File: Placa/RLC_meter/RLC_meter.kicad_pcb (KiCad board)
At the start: 2 copper layers, 12 parts, among them J1 BAT, J2 BAT, Q1 IRF4905, Q2 IRF4905, U3 L7805, U4 LM358

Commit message: massive update. Local to git
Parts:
- removed Q1, Q2: IRF4905, Package_TO_SOT_THT:TO-220-3_Vertical
- removed REF**: TP4056 module, RLC_meter:TP4056
- added C3: 100n, Capacitor_THT:C_Disc_D5.0mm_W2.5mm_P2.50mm, F.Cu at (34.0, 63.8)
- added C4: 100n, Capacitor_THT:C_Disc_D5.0mm_W2.5mm_P2.50mm, F.Cu at (43.0, 63.8)
- added C5: 100u, Capacitor_THT:CP_Radial_D8.0mm_P5.00mm, F.Cu at (47.1, 64.5)
- added J3: HC05, Connector_PinHeader_2.54mm:PinHeader_1x04_P2.54mm_Horizontal, F.Cu at (94.6, 22.7)
- added J4: Load_terminal, TerminalBlock_Philmore:TerminalBlock_Philmore_TB132_1x02_P5.00mm_Horizontal, F.Cu at (31.2, 37.0)
- added R4: 100k, Resistor_THT:R_Axial_DIN0309_L9.0mm_D3.2mm_P15.24mm_Horizontal, F.Cu at (55.9, 23.0)
- added R5: 560, Resistor_THT:R_Axial_DIN0309_L9.0mm_D3.2mm_P15.24mm_Horizontal, F.Cu at (60.0, 26.9)
- added R6: 560, Resistor_THT:R_Axial_DIN0309_L9.0mm_D3.2mm_P15.24mm_Horizontal, F.Cu at (89.1, 23.0)
- added RV1: 50k, Potentiometer_THT:Potentiometer_Bourns_3386C_Horizontal, F.Cu at (49.5, 27.5)
- added U1: LPC845, RLC_meter:LPC845, F.Cu at (80.8, 56.9)
- added U2: X9Cxxx, Package_DIP:DIP-8_W7.62mm_Socket_LongPads, F.Cu at (85.3, 34.7)
- added U5: AMS1117-3.3, Connector_PinHeader_2.54mm:PinHeader_1x03_P2.54mm_Vertical, F.Cu at (47.0, 43.5)
- C1, C2: value C -> 100n; footprint Capacitor_THT:C_Axial_L5.1mm_D3.1mm_P7.50mm_Horizontal -> Capacitor_THT:C_Disc_D5.0mm_W2.5mm_P2.50mm
- J1: value BAT -> Batt1
- J2: value BAT -> Batt2
- R1: value R -> 150k; footprint Resistor_THT:R_Axial_DIN0207_L6.3mm_D2.5mm_P10.16mm_Horizontal -> Resistor_THT:R_Axial_DIN0309_L9.0mm_D3.2mm_P15.24mm_Horizontal
- R2: value R -> 220k; footprint Resistor_THT:R_Axial_DIN0207_L6.3mm_D2.5mm_P10.16mm_Horizontal -> Resistor_THT:R_Axial_DIN0309_L9.0mm_D3.2mm_P15.24mm_Horizontal
- R3: value R -> 100k; footprint Resistor_THT:R_Axial_DIN0207_L6.3mm_D2.5mm_P10.16mm_Horizontal -> Resistor_THT:R_Axial_DIN0309_L9.0mm_D3.2mm_P15.24mm_Horizontal
- U3: value L7805 -> MC33202; footprint Package_TO_SOT_THT:TO-220-3_Horizontal_TabDown -> Package_DIP:DIP-8_W7.62mm_Socket_LongPads
- U4: value LM358 -> L7805; footprint Package_DIP:DIP-8_W7.62mm -> Package_TO_SOT_THT:TO-220-3_Horizontal_TabDown
- moved J2 65.7 mm to (29.0, 48.3), turned to 180 degrees
- moved C1 59.2 mm to (38.5, 63.8), turned to -90 degrees
- moved R1 57.7 mm to (28.4, 27.0)
- moved J1 54.0 mm to (29.0, 55.2)
- moved U4 40.1 mm to (35.5, 60.2)
- moved R2 32.1 mm to (43.6, 23.0), turned to 180 degrees
- moved R3 31.1 mm to (63.9, 30.0)
- moved C2 26.2 mm to (45.5, 57.0), turned to -90 degrees
- moved U3 25.1 mm to (72.0, 34.2), turned to -90 degrees
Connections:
- C1 pad 1: +BATT -> +5V
- C2 pad 1: VCC -> +3.3V
- J1 pad 1: Net-(J1-Pad1) -> +BATT
- J1 pad 2: /in_BAT2- -> GND
- J2 pad 1: Net-(J2-Pad1) -> GND
- J2 pad 2: /in_BAT1- -> -BATT
- R2 pad 2: /Signal_o -> -BATT
- R3 pad 1: /Singal_i -> Net-(R3-Pad1)
- R3 pad 2: /Signal_o -> /V_DAC
- U3 pad 1: +BATT -> /Signal_i
- U3 pad 2: GND -> Net-(R3-Pad1)
- U3 pad 3: VCC -> GND
- U4 pad 1: /Signal_o -> +BATT
- U4 pad 2: Net-(R1-Pad2) -> GND
- U4 pad 3: /DAC -> +5V
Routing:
- net +5V: track 0.00 -> 202.0 mm, vias 0 -> 2
- net /Signal_i: track 0.00 -> 112.6 mm
- net /V_DAC: track 0.00 -> 99.1 mm, vias 0 -> 2
- net +BATT: track 0.00 -> 73.5 mm
- net -BATT: track 0.00 -> 69.8 mm
- net /RX: track 0.00 -> 69.4 mm
- net /TX: track 0.00 -> 66.1 mm
- net Net-(R3-Pad1): track 0.00 -> 40.8 mm
- net /generated_signal: track 0.00 -> 37.5 mm
- net /POT+: track 0.00 -> 33.1 mm
- net +3.3V: track 0.00 -> 23.6 mm
- net /POT_V: track 0.00 -> 19.7 mm
- net /POT_U/D: track 0.00 -> 19.3 mm
- net /POT_INC: track 0.00 -> 17.9 mm
- net Net-(R1-Pad2): track 0.00 -> 10.1 mm
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- added copper zone on B.Cu, net GND
- added copper zone on F.Cu, net GND
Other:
- board outline added: 90 x 50 mm

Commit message: correxiones en clase
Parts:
- moved C2 13.0 mm to (58.4, 55.9)
- moved R6 6.57 mm to (82.5, 23.0)
- moved R4 6.35 mm to (49.5, 23.0)
- moved J3 5.02 mm to (89.6, 22.7)
- moved C3 2.95 mm to (31.1, 63.5)
- moved C1 2.95 mm to (35.6, 63.5)
- moved C4 2.95 mm to (40.1, 63.5)
- moved C5 2.51 mm to (44.6, 64.5)
- moved R3 2.06 mm to (63.9, 27.9)
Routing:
- net +5V: track 202.0 -> 223.9 mm
- net /RX: track 69.4 -> 85.0 mm
- net /TX: track 66.1 -> 81.7 mm
- net /Signal_i: track 112.6 -> 120.9 mm
- net +3.3V: track 23.6 -> 19.5 mm
- net /POT+: track 33.1 -> 35.8 mm
- net Net-(R3-Pad1): track 40.8 -> 43.0 mm
- net /V_DAC: track 99.1 -> 101.3 mm, vias 2 -> 0
- net Net-(R1-Pad2): track 10.1 -> 11.7 mm
- net +BATT: track 73.5 -> 74.6 mm

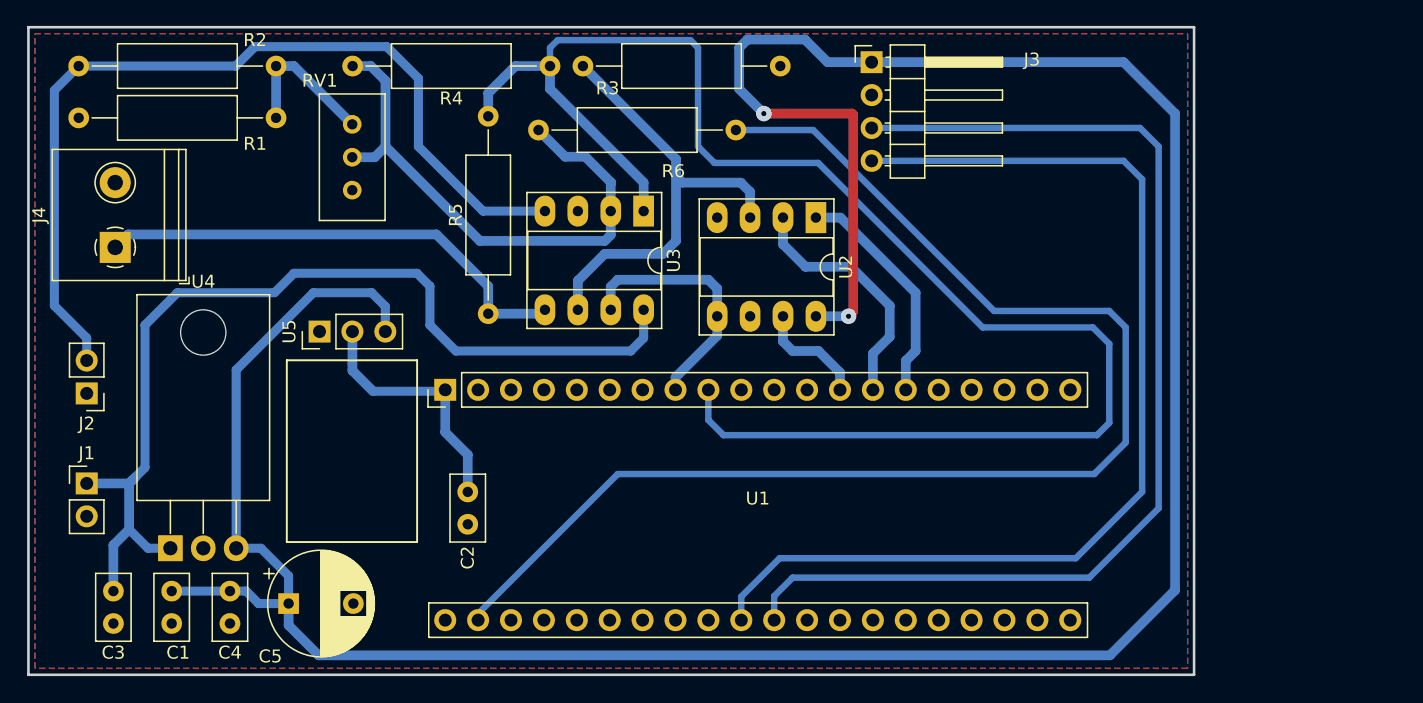
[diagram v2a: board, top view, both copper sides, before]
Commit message: fixed frecuency, single letter command, general revision
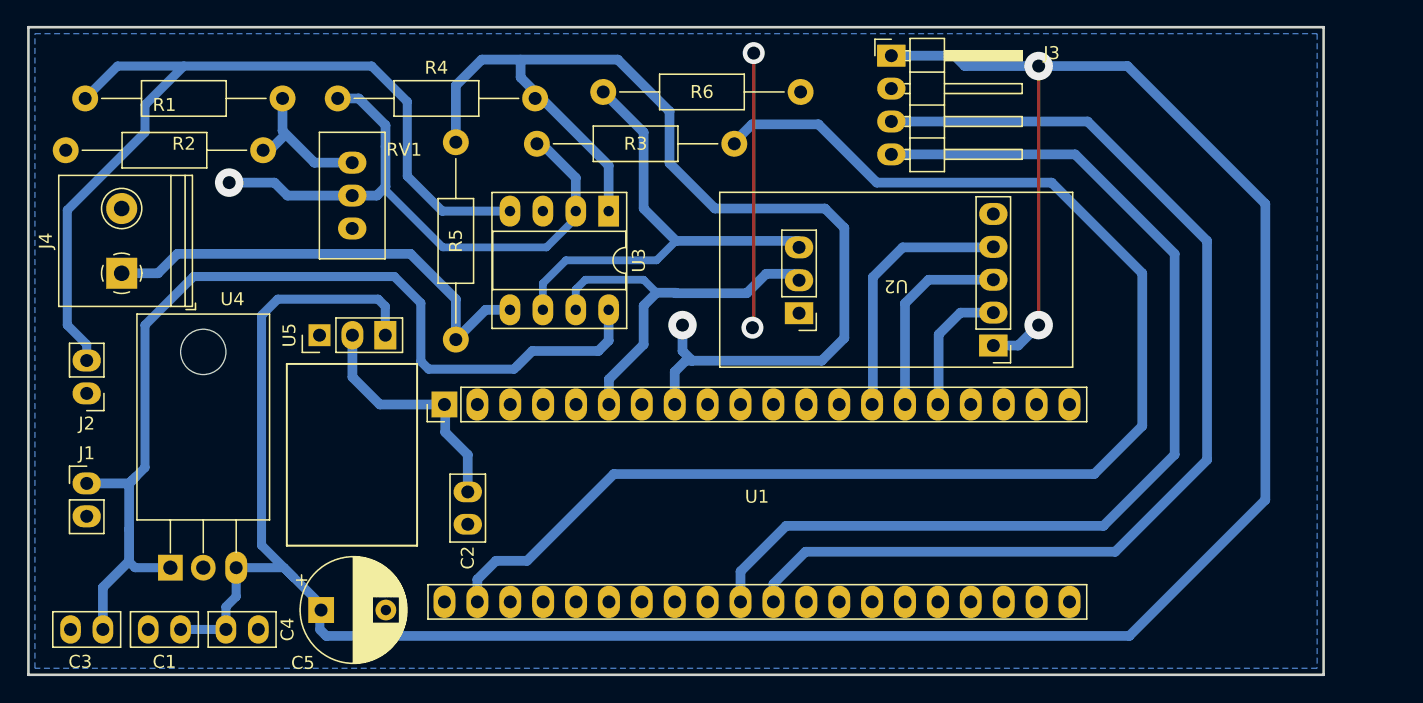
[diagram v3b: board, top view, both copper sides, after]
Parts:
- R1, R2, R3, R4, R5: footprint Resistor_THT:R_Axial_DIN0309_L9.0mm_D3.2mm_P15.24mm_Horizontal -> Resistor_THT:R_Axial_DIN0207_L6.3mm_D2.5mm_P15.24mm_Horizontal
- R6: value 560 -> 33; footprint Resistor_THT:R_Axial_DIN0309_L9.0mm_D3.2mm_P15.24mm_Horizontal -> Resistor_THT:R_Axial_DIN0207_L6.3mm_D2.5mm_P15.24mm_Horizontal
- U2: footprint Package_DIP:DIP-8_W7.62mm_Socket_LongPads -> RLC_meter:X9Cxxx
- moved U2 7.84 mm to (91.5, 39.5), turned to 180 degrees
- moved R5 3.20 mm to (57.5, 28.9)
- moved C3 3.07 mm to (30.2, 66.5), turned to 180 degrees
- moved C1 3.04 mm to (36.2, 66.5), turned to 180 degrees
- moved C4 2.98 mm to (39.8, 66.5), turned to 0 degrees
- moved RV1 2.96 mm to (49.5, 30.5)
- moved R4 2.75 mm to (48.4, 25.5)
- moved U3 2.70 mm to (69.3, 34.2)
- moved R1 2.69 mm to (27.4, 29.5)
- moved C5 2.56 mm to (47.1, 65.0)
- moved R2 2.55 mm to (44.1, 25.5)
- moved R6 2.54 mm to (84.1, 25.0)
- moved J4 2.06 mm to (31.7, 39.0)
- moved J3 1.60 mm to (91.1, 22.2)
- moved U4 1.50 mm to (35.5, 61.7)
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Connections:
- U1 pad 25: unconnected-(U1-Pad25) -> /POT_CS
- U1 pad 28: /POT_CS -> unconnected-(U1-Pad28)
- U1 pad 32: /Signal_i -> unconnected-(U1-Pad32)
- U1 pad 33: /POT_V -> /Signal_i
- U1 pad 35: unconnected-(U1-Pad35) -> /POT_V
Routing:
- net /Signal_i: track 120.9 -> 85.7 mm, vias 0 -> 1
- net GND: track 0.00 -> 21.2 mm, vias 0 -> 2
- net /POT_V: track 19.7 -> 37.3 mm
- net +5V: track 223.9 -> 209.9 mm
- net Net-(R3-Pad1): track 43.0 -> 50.1 mm, vias 0 -> 1
- net +BATT: track 74.6 -> 80.6 mm
- net /V_DAC: track 101.3 -> 106.4 mm
- net /POT_INC: track 17.9 -> 14.9 mm
- net /generated_signal: track 37.5 -> 35.6 mm
- net /POT_CS: track 8.67 -> 10.4 mm
- net /TX: track 81.7 -> 80.2 mm
- net /POT+: track 35.8 -> 37.0 mm
- net /RX: track 85.0 -> 83.9 mm
- net /POT_U/D: track 19.3 -> 20.1 mm
- net Net-(R1-Pad2): track 11.7 -> 11.0 mm
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- removed copper zone on F.Cu, net GND
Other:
- board size 90 x 50 mm -> 100 x 50 mm

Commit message: update code
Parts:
- moved R6 0.64 mm to (84.6, 25.4)
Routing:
- net /V_DAC: track 106.4 -> 105.0 mm
- net /Signal_i: track 85.7 -> 84.4 mm
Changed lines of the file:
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@@
   )
   (footprint "Resistor_THT:R_Axial_DIN0207_L6.3mm_D2.5mm_P15.24mm_Horizontal" (layer "F.Cu")
-    (at 84.12 25 180)
+    (at 84.62 25.4 180)
     (descr "Resistor, Axial_DIN0207 series, Axial, Horizontal, pin pitch=15.24mm, 0.25W = 1/4W, length*diameter=6.3*2.5mm^2, http://cdn-reichelt.de/documents/datenblatt/B400/1_4W%23YAG.pdf")
     (tags "Resistor Axial_DIN0207 series Axial Horizontal pin pitch 15.24mm 0.25W = 1/4W length 6.3mm diameter 2.5mm")
@@
   (segment (start 66.76 31.63) (end 66.76 34.2) (width 0.75) (layer "B.Cu") (net 10))
   (segment (start 52.07 32.57) (end 56.5 37) (width 0.6) (layer "B.Cu") (net 10))
+  (segment (start 69.7 54.5) (end 106.79 54.5) (width 0.75) (layer "B.Cu") (net 11))
+  (segment (start 110.5 39) (end 103.5 32) (width 0.75) (layer "B.Cu") (net 11))
+  (segment (start 110.5 50.79) (end 110.5 39) (width 0.75) (layer "B.Cu") (net 11))
+  (segment (start 59.16 64.37) (end 59.16 62.64) (width 0.75) (layer "B.Cu") (net 11))
+  (segment (start 90 32) (end 87 29) (width 0.75) (layer "B.Cu") (net 11))
   (segment (start 63 61.2) (end 69.7 54.5) (width 0.75) (layer "B.Cu") (net 11))
-  (segment (start 110.5 50.79) (end 110.5 39) (width 0.75) (layer "B.Cu") (net 11))
-  (segment (start 80.37 27.5) (end 79.12 28.75) (width 0.75) (layer "B.Cu") (net 11))
+  (segment (start 103.5 32) (end 90 32) (width 0.75) (layer "B.Cu") (net 11))
+  (segment (start 87 29) (end 79.37 29) (width 0.75) (layer "B.Cu") (net 11))
   (segment (start 59.16 62.64) (end 60.6 61.2) (width 0.75) (layer "B.Cu") (net 11))
-  (segment (start 110.5 39) (end 103.5 32) (width 0.75) (layer "B.Cu") (net 11))
-  (segment (start 59.16 64.37) (end 59.16 62.64) (width 0.75) (layer "B.Cu") (net 11))
-  (segment (start 69.7 54.5) (end 106.79 54.5) (width 0.75) (layer "B.Cu") (net 11))
-  (segment (start 90 32) (end 85.5 27.5) (width 0.75) (layer "B.Cu") (net 11))
   (segment (start 106.79 54.5) (end 110.5 50.79) (width 0.75) (layer "B.Cu") (net 11))
-  (segment (start 103.5 32) (end 90 32) (width 0.75) (layer "B.Cu") (net 11))
   (segment (start 60.6 61.2) (end 63 61.2) (width 0.75) (layer "B.Cu") (net 11))
-  (segment (start 85.5 27.5) (end 80.37 27.5) (width 0.75) (layer "B.Cu") (net 11))
   (via (at 75 43) (size 2.2) (drill 1) (layers "F.Cu" "B.Cu") (free) (net 12))
   (segment (start 75.25 45.75) (end 75.75 45.75) (width 0.75) (layer "B.Cu") (net 12))
-  (segment (start 69.3 34.2) (end 69.3 30.68) (width 0.75) (layer "B.Cu") (net 12))
+  (segment (start 58.8 23.2) (end 57.5 24.5) (width 0.75) (layer "B.Cu") (net 12))
+  (segment (start 69.3 31.18) (end 62.5 24.38) (width 0.75) (layer "B.Cu") (net 12))
+  (segment (start 69.3 34.2) (end 69.3 31.18) (width 0.75) (layer "B.Cu") (net 12))
   (segment (start 87.5 35.5) (end 86 34) (width 0.75) (layer "B.Cu") (net 12))
-  (segment (start 69.3 30.68) (end 62.5 23.88) (width 0.75) (layer "B.Cu") (net 12))
-  (segment (start 74 26.5) (end 70 22.5) (width 0.75) (layer "B.Cu") (net 12))
+  (segment (start 86 34) (end 77.5 34) (width 0.75) (layer "B.Cu") (net 12))
+  (segment (start 75.75 45.75) (end 85.75 45.75) (width 0.75) (layer "B.Cu") (net 12))
   (segment (start 74.4 46.6) (end 75.25 45.75) (width 0.75) (layer "B.Cu") (net 12))
   (segment (start 75 45) (end 75.75 45.75) (width 0.75) (layer "B.Cu") (net 12))
+  (segment (start 57.5 24.5) (end 57.5 28.88) (width 0.75) (layer "B.Cu") (net 12))
+  (segment (start 77.5 34) (end 74 30.5) (width 0.75) (layer "B.Cu") (net 12))
+  (segment (start 74.4 46.6) (end 74.4 49.13) (width 0.75) (layer "B.Cu") (net 12))
+  (segment (start 85.75 45.75) (end 87.5 44) (width 0.75) (layer "B.Cu") (net 12))
+  (segment (start 70.7 23.2) (end 58.8 23.2) (width 0.75) (layer "B.Cu") (net 12))
+  (segment (start 75 43) (end 75 45) (width 0.75) (layer "B.Cu") (net 12))
+  (segment (start 87.5 44) (end 87.5 35.5) (width 0.75) (layer "B.Cu") (net 12))
   (segment (start 74 30.5) (end 74 26.5) (width 0.75) (layer "B.Cu") (net 12))
-  (segment (start 75.75 45.75) (end 85.75 45.75) (width 0.75) (layer "B.Cu") (net 12))
-  (segment (start 70 22.5) (end 59.5 22.5) (width 0.75) (layer "B.Cu") (net 12))
-  (segment (start 87.5 44) (end 87.5 35.5) (width 0.75) (layer "B.Cu") (net 12))
-  (segment (start 86 34) (end 77.5 34) (width 0.75) (layer "B.Cu") (net 12))
-  (segment (start 74.4 46.6) (end 74.4 49.13) (width 0.75) (layer "B.Cu") (net 12))
-  (segment (start 59.5 22.5) (end 57.5 24.5) (width 0.75) (layer "B.Cu") (net 12))
-  (segment (start 77.5 34) (end 74 30.5) (width 0.75) (layer "B.Cu") (net 12))
-  (segment (start 75 43) (end 75 45) (width 0.75) (layer "B.Cu") (net 12))
-  (segment (start 62.5 23.88) (end 62.5 22.5) (width 0.75) (layer "B.Cu") (net 12))
-  (segment (start 57.5 24.5) (end 57.5 28.88) (width 0.75) (layer "B.Cu") (net 12))
-  (segment (start 85.75 45.75) (end 87.5 44) (width 0.75) (layer "B.Cu") (net 12))
+  (segment (start 62.5 24.38) (end 62.5 23.2) (width 0.75) (layer "B.Cu") (net 12))
+  (segment (start 74 26.5) (end 70.7 23.2) (width 0.75) (layer "B.Cu") (net 12))
   (segment (start 74.5 36.5) (end 72 34) (width 0.75) (layer "B.Cu") (net 13))
   (segment (start 72 28.12) (end 68.88 25) (width 0.75) (layer "B.Cu") (net 13))
@@
     (polygon
       (pts
-        (xy 124 69.5)
-        (xy 25 69.5)
-        (xy 25 20.5)
-        (xy 124 20.5)
+        (xy 124.4 70)
+        (xy 24.6 70)
+        (xy 24.6 20)
+        (xy 124.4 20)
       )
     )
